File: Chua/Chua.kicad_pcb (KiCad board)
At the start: 2 copper layers, 60 x 80 mm, 19 parts, among them P1 CONN_01X03, U1 TL082, U2 TL082

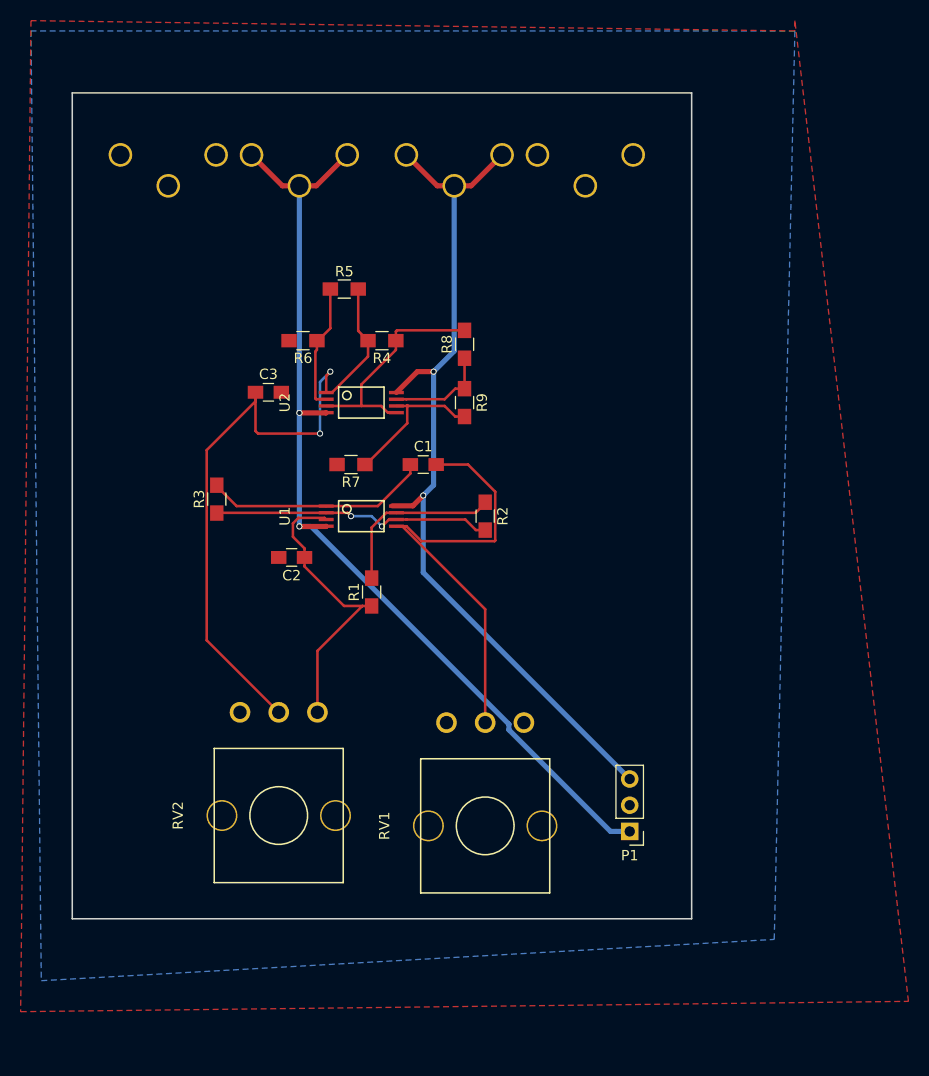
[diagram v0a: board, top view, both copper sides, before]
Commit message: chua redesigned board for smallerness
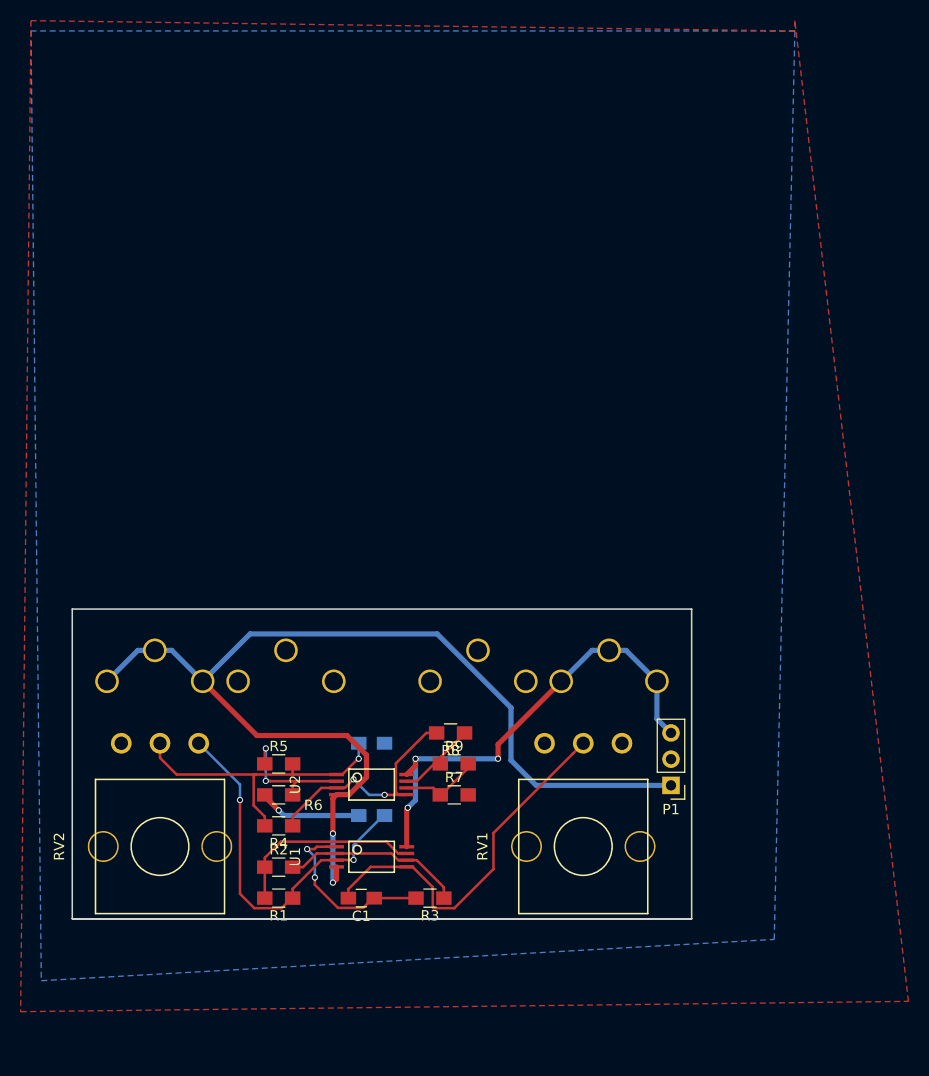
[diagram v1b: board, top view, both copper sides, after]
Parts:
- C2, C3: moved to B.Cu
- moved BT1 48.1 mm to (115.7, 125.5), turned to 180 degrees
- moved R4 48.1 mm to (90.0, 141.0)
- moved BT2 48.0 mm to (84.3, 125.5), turned to 180 degrees
- moved R5 46.4 mm to (90.0, 135.0)
- moved R6 44.1 mm to (90.0, 138.0)
- moved R3 43.8 mm to (104.7, 148.0), turned to 180 degrees
- moved C1 42.4 mm to (98.0, 148.0), turned to 180 degrees
- moved R2 39.4 mm to (90.0, 145.0), turned to 0 degrees
- moved R8 37.7 mm to (106.7, 132.0), turned to 180 degrees
- moved U2 37.0 mm to (99.0, 137.0)
- moved C3 35.4 mm to (99.0, 133.0)
- moved R9 35.0 mm to (107.0, 135.0), turned to 0 degrees
- moved R7 33.5 mm to (107.0, 138.0), turned to 0 degrees
- moved U1 33.0 mm to (99.0, 144.0)
- moved R1 31.0 mm to (90.0, 148.0), turned to 180 degrees
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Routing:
- net /VCC+: track 86.6 -> 46.1 mm, vias 2 -> 3
- net Net-(C3-Pad1): track 67.0 -> 30.1 mm, vias 2 -> 1
- net GND: track 0.00 -> 10.0 mm, vias 0 -> 1
- net Net-(R2-Pad2): track 27.3 -> 17.6 mm, vias 2 -> 0
- net Net-(C1-Pad2): track 45.0 -> 36.0 mm
- net /VCC-: track 94.5 -> 103.0 mm
- net Net-(C2-Pad1): track 28.3 -> 35.9 mm, vias 0 -> 2
- net Net-(R7-Pad1): track 14.6 -> 7.71 mm
- net Net-(C1-Pad1): track 21.8 -> 17.8 mm, vias 0 -> 2
- net Net-(R1-Pad2): track 17.0 -> 18.8 mm
- net Net-(R8-Pad1): track 9.97 -> 8.38 mm
- net Net-(R4-Pad1): track 22.4 -> 23.2 mm, vias 0 -> 2
- net Net-(R5-Pad1): track 12.3 -> 13.1 mm, vias 0 -> 2
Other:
- board size 60 x 80 mm -> 60 x 30 mm

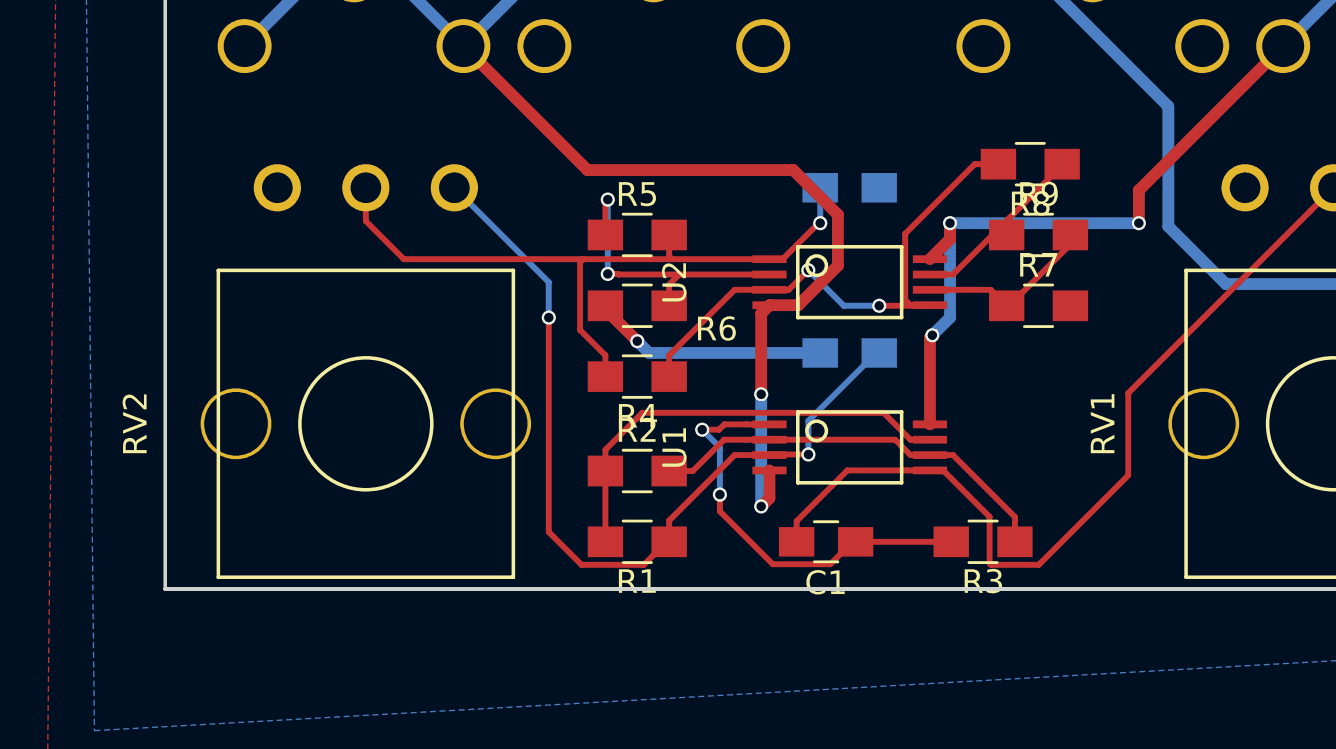
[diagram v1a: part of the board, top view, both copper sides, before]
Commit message: added label to chua
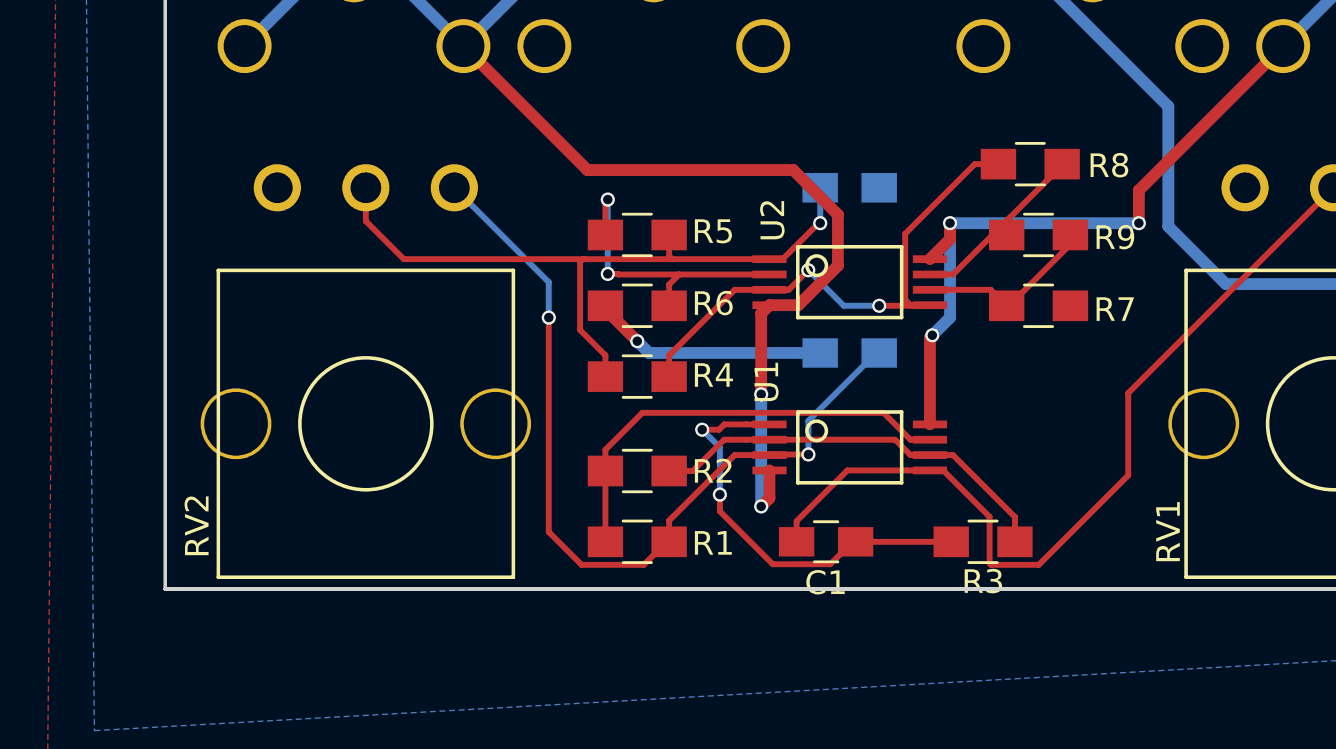
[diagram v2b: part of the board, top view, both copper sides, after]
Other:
- board text added: "Chua Circuit DM053117"

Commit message: adding output to chua
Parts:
- added P2: CONN_01X04, Pin_Headers:Pin_Header_Straight_1x04_Pitch2.54mm, F.Cu at (95.9, 151.0)
- moved P1 29.9 mm to (100.0, 126.6)
- moved RV1 2.00 mm to (121.5, 143.0)
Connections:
- net Net-(C2-Pad1) renamed /X
- net Net-(C3-Pad1) renamed /Y
- net Net-(R1-Pad2) renamed /P
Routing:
- net /VCC-: track 103.0 -> 71.1 mm
- net /VCC+: track 46.1 -> 63.6 mm
- net /Y: track 30.1 -> 45.0 mm, vias 1 -> 2
- net /P: track 18.8 -> 29.9 mm, vias 0 -> 1
- net /X: track 35.9 -> 42.2 mm
- net Net-(C1-Pad2): track 36.0 -> 32.9 mm, vias 0 -> 1
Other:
- board outline removed

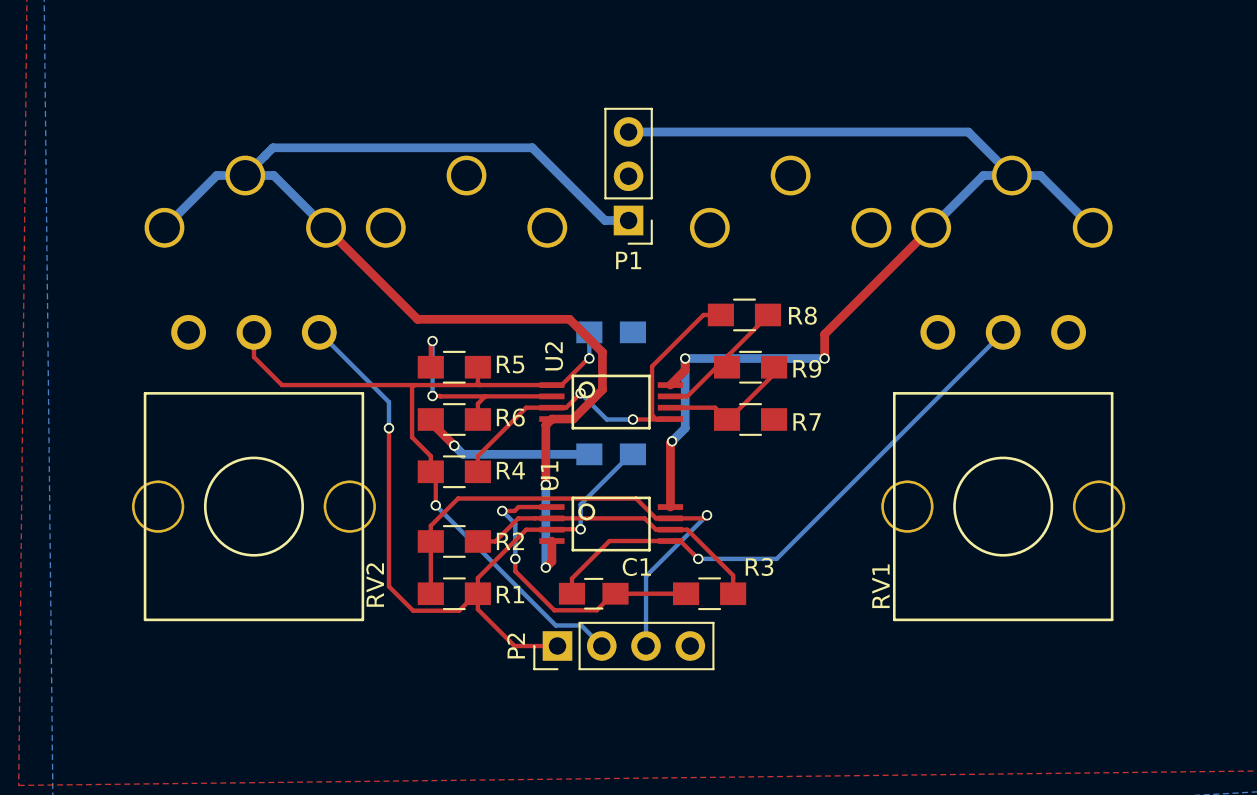
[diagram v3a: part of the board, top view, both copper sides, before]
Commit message: fixed incorrect chua diode connection
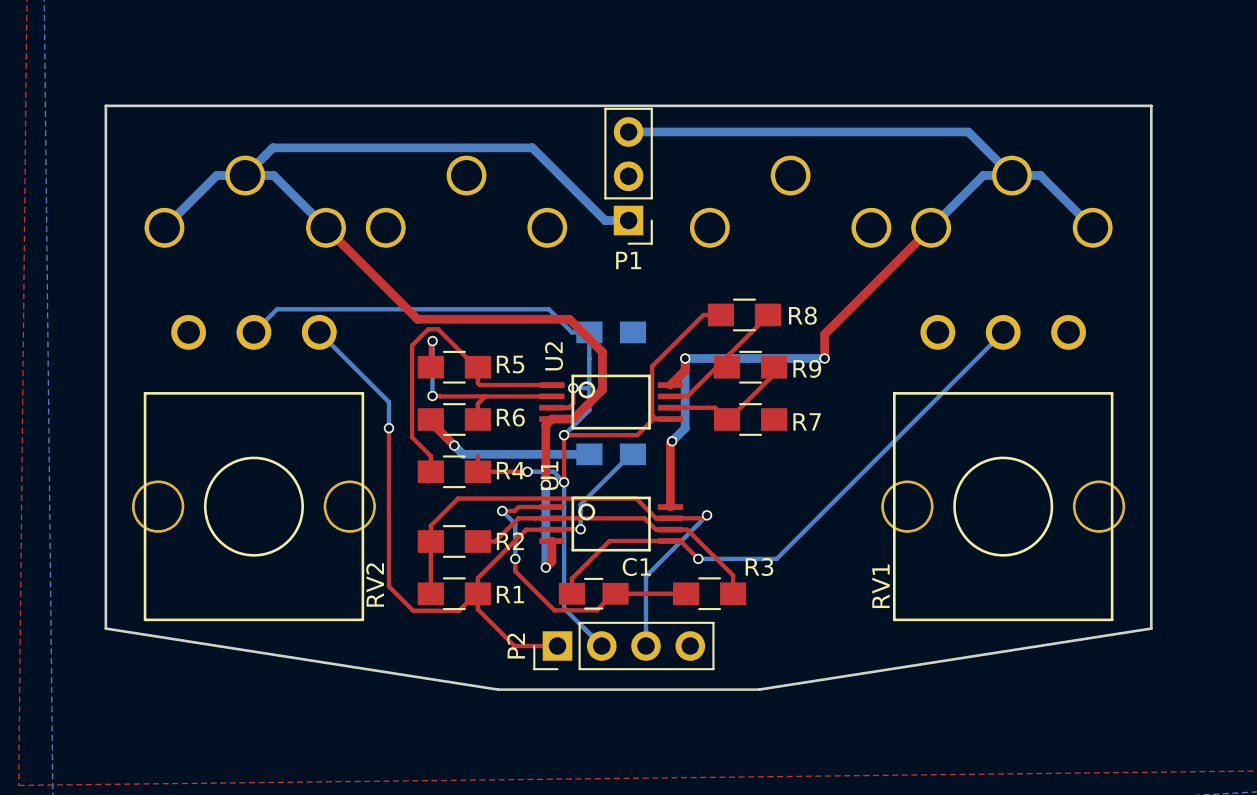
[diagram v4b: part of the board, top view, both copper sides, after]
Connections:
- R4 pad 1: Net-(R4-Pad1) -> /Y
- R4 pad 2: /Y -> Net-(R4-Pad2)
- R5 pad 2: /Y -> Net-(R4-Pad2)
- R8 pad 2: Net-(R4-Pad1) -> /Y
- U2 pad 1: /Y -> Net-(R4-Pad2)
- U2 pad 3: Net-(R4-Pad1) -> /Y
- U2 pad 5: Net-(R4-Pad1) -> /Y
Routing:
- net Net-(R4-Pad1): track 23.2 -> 0.00 mm, vias 2 -> 0
- net /Y: track 45.0 -> 67.2 mm, vias 2 -> 4
- net Net-(R4-Pad2): track 0.00 -> 18.9 mm
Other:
- board outline added: 60 x 33.5 mm
- rule pad_to_mask_clearance: 0.2 -> 0
